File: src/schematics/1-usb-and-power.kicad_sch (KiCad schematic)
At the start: 0 parts

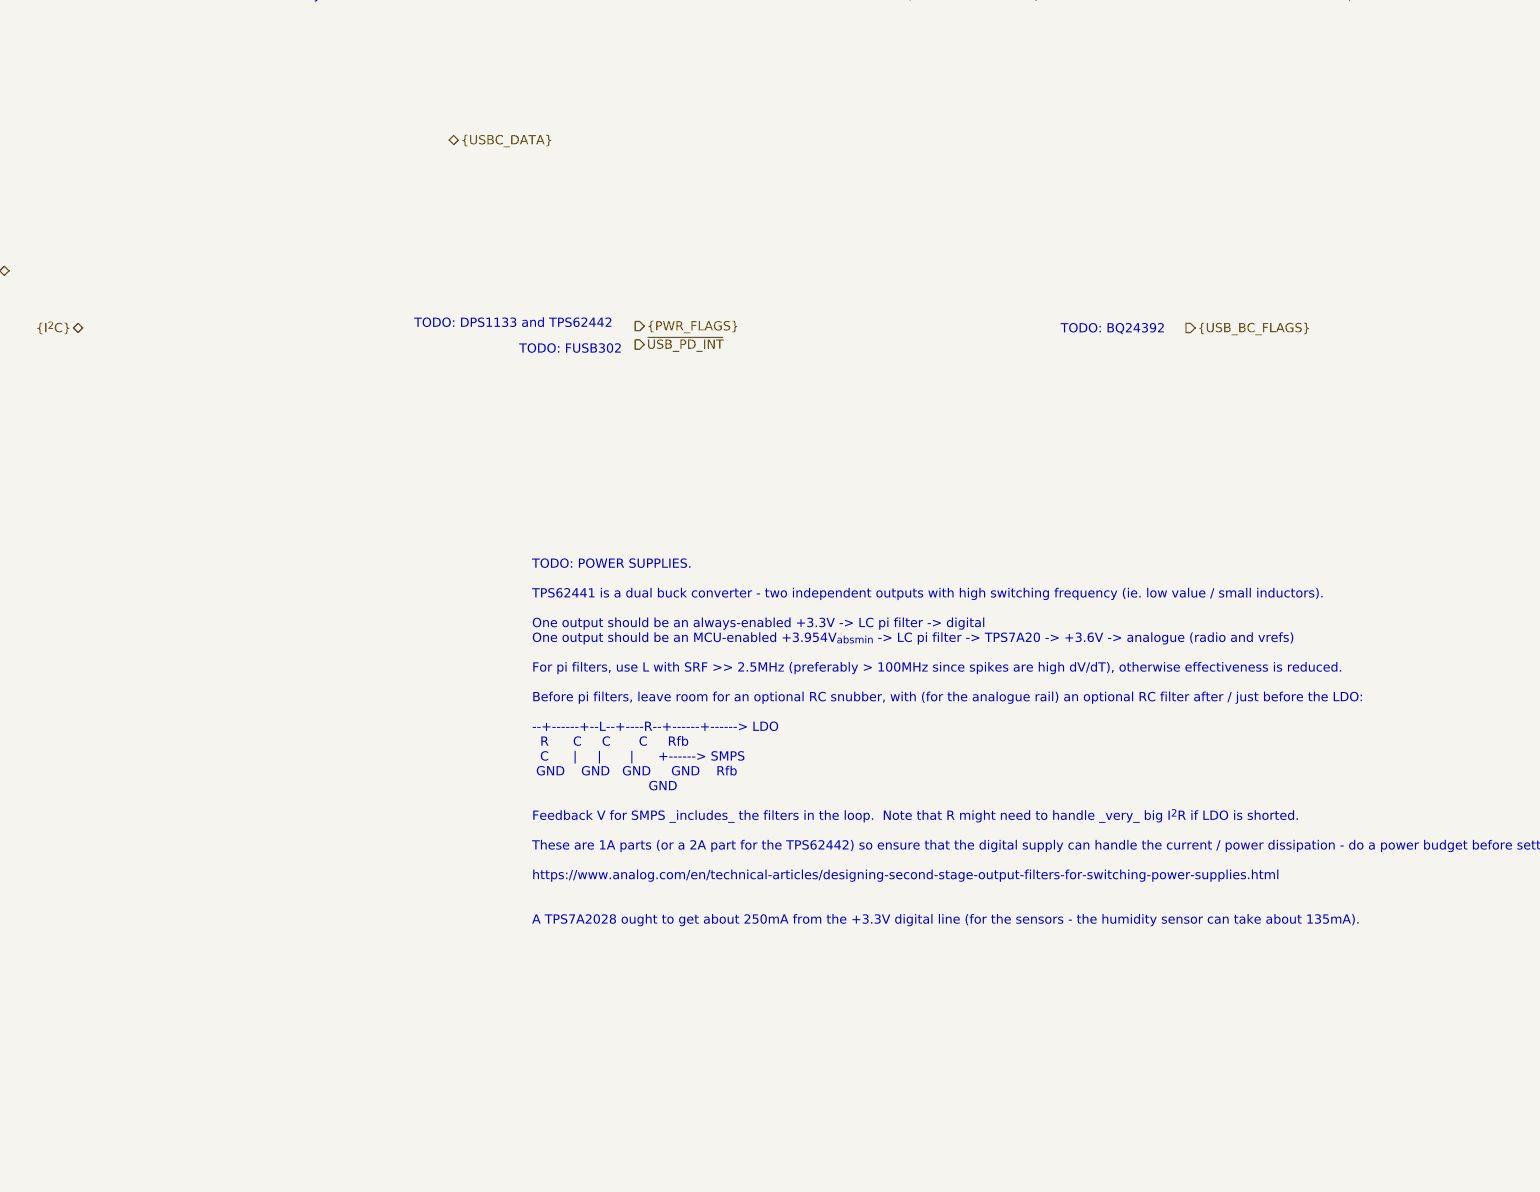
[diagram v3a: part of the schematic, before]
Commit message: Further elaboration of the design and schematics, mainly power supply calculations.
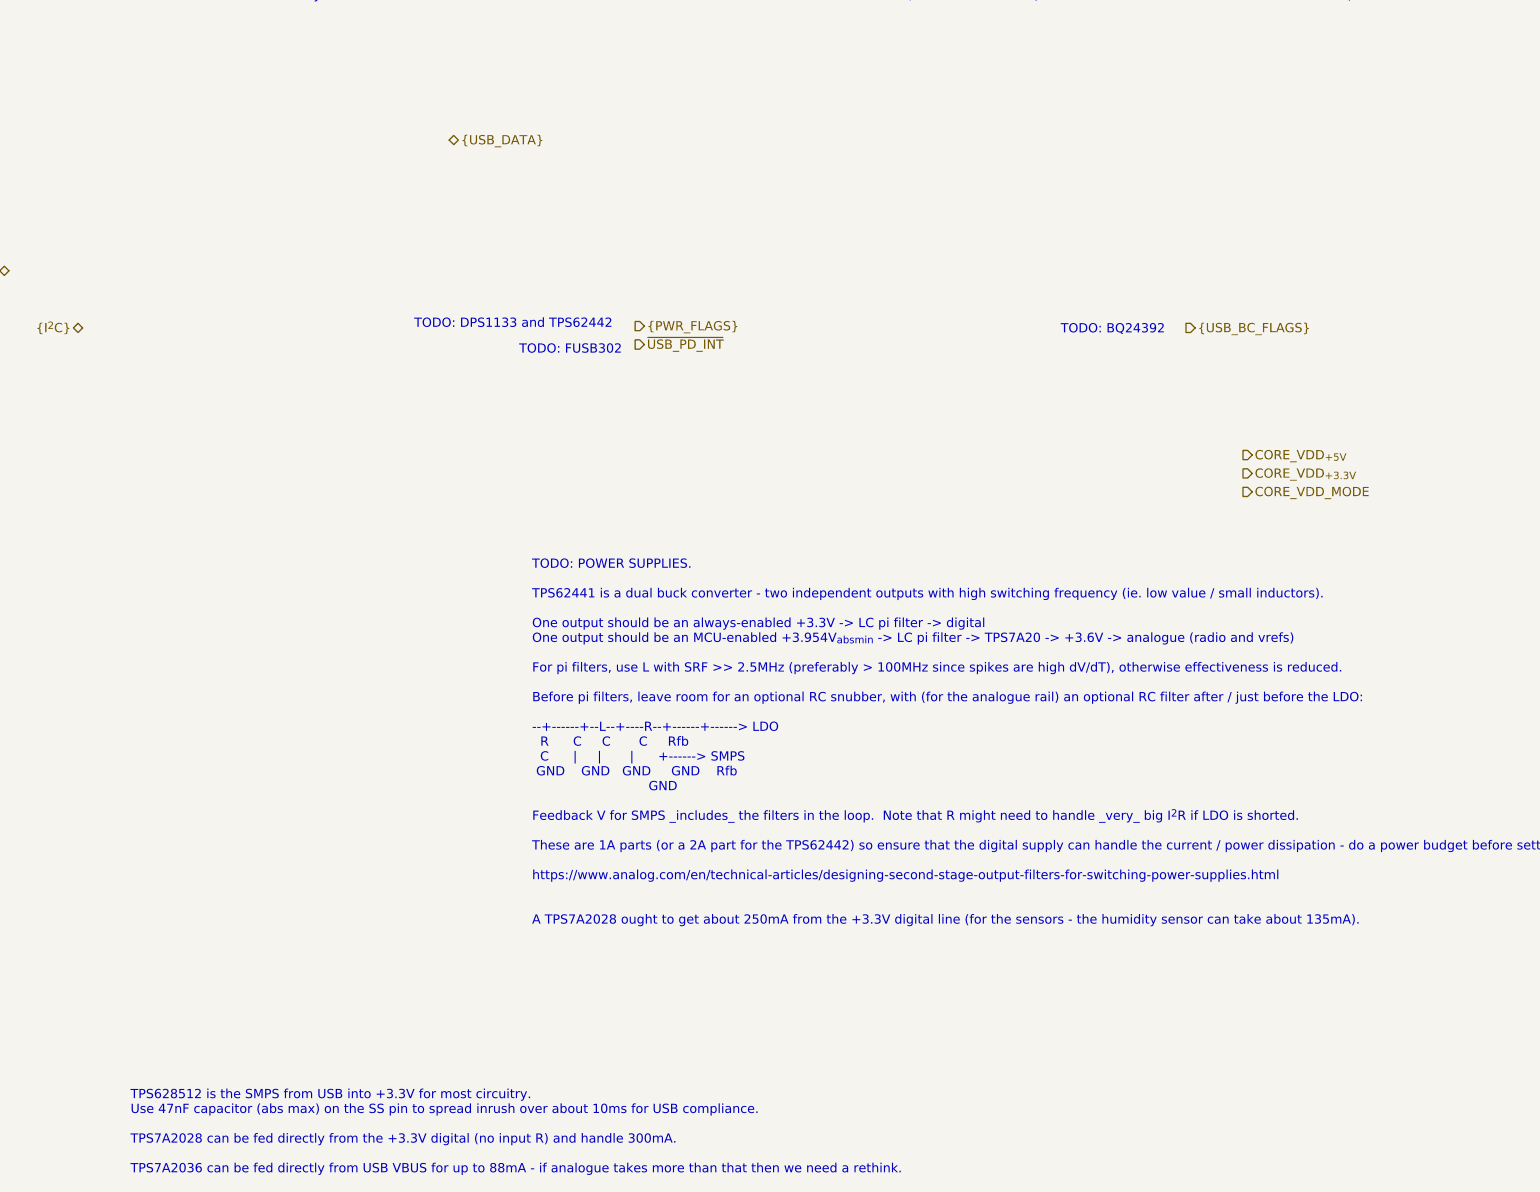
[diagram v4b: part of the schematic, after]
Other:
- note added: "TPS628512 is the SMPS from USB into +3.3V for most circuitry. Use 47nF capacitor (abs max) on the SS pin to spread inrush over about 10ms for USB compliance. TPS7A2028 can be fed directly from the +3.3V digital (no input R) and handle 300mA. TPS7A2036 can be fed directly from USB VBUS for up to 88mA - if analogue takes more than that then we need a rethink."
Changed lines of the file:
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@@
+    (effects (font (size 1.27 1.27)) (justify left bottom))
+  )
+  (text "TPS628512 is the SMPS from USB into +3.3V for most circuitry.\nUse 47nF capacitor (abs max) on the SS pin to spread inrush over about 10ms for USB compliance.\n\nTPS7A2028 can be fed directly from the +3.3V digital (no input R) and handle 300mA.\n\nTPS7A2036 can be fed directly from USB VBUS for up to 88mA - if analogue takes more than that then we need a rethink.\n"
+    (at 82.804 244.094 0)
     (effects (font (size 1.27 1.27)) (justify left bottom))
   )
@@
     (effects (font (size 1.27 1.27)) (justify right))
   )
-  (hierarchical_label "{USBC_DATA}" (shape bidirectional) (at 126.746 101.346 0) (fields_autoplaced)
+  (hierarchical_label "CORE_VDD_MODE" (shape output) (at 236.22 149.86 0) (fields_autoplaced)
     (effects (font (size 1.27 1.27)) (justify left))
   )
+  (hierarchical_label "CORE_VDD_{+3.3V}" (shape output) (at 236.22 147.32 0) (fields_autoplaced)
+    (effects (font (size 1.27 1.27)) (justify left))
+  )
+  (hierarchical_label "{USB_DATA}" (shape bidirectional) (at 126.746 101.346 0) (fields_autoplaced)
+    (effects (font (size 1.27 1.27)) (justify left))
+  )
+  (hierarchical_label "CORE_VDD_{+5V}" (shape output) (at 236.22 144.78 0) (fields_autoplaced)
+    (effects (font (size 1.27 1.27)) (justify left))
+  )

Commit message: Started to draw the USB / power input module.
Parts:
- added C23: 100nF, restall-generic-capacitors:unpolarised-nominal-0402-1005, symbol restall-generic-capacitors:capacitor-unpolarised
- added C24: DNP, restall-generic-capacitors:unpolarised-nominal-0402-1005, symbol restall-generic-capacitors:capacitor-unpolarised
- added C25: 360nF, restall-generic-capacitors:unpolarised-nominal-0402-1005, symbol restall-generic-capacitors:capacitor-unpolarised
- added C26: 100pF, restall-generic-capacitors:unpolarised-nominal-0402-1005, symbol restall-generic-capacitors:capacitor-unpolarised
- added C27, C28: 4.7μF, restall-generic-capacitors:unpolarised-nominal-0805-2012, symbol restall-generic-capacitors:capacitor-unpolarised
- added FB101: WLBD2012HCU121TH, restall-manufacturer-walsin:WLBD2012, symbol restall-manufacturer-walsin:WLBD2012HCU121TH
- added R21: 300kΩ, restall-generic-resistors:nominal-0402-1005, symbol restall-generic-resistors:resistor
- added R22: 0Ω, restall-generic-resistors:nominal-0402-1005, symbol restall-generic-resistors:resistor
- added R23: 1kΩ, restall-generic-resistors:nominal-0402-1005, symbol restall-generic-resistors:resistor
- added U2: MP5016HGQH, restall-manufacturer-mps:QFN10-1.5x2.0mm-0.5mm, symbol restall-manufacturer-mps:MP5016HGQH
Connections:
- net CORE_VDD_{+5V}: now also U2.6 (SOURCE)
- net USBC_VBUS: now also C27.1, FB101.1 (P1)
- new net: C26.1, U2.8 (GATE)
- new net: R23.1, U2.4 (ILIMIT)
- new net: C25.1, U2.10 (DV/DT)
- new net: C28.1, FB101.2 (P2), R21.1, U2.1 (V_{CC})
- new net: C23.1, R21.2, U2.9 (EN)
- new net: C24.1, R22.1, U2.5 (MODE)
- new net GND: C23.2, C24.2, C25.2, C26.2, C27.2, C28.2, R22.2, R23.2, U2.3 (GND)
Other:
- note added: "OVP_{typ}=5.75V [5.5V,6V] OCP_{typ}=2.1A"
- note added: "Ramp_{typ}=48ms; must be at least 20ms to keep USB inrush below 100mA"
- note added: "TODO: CHECK OCP LIMIT OF 2.1A IS SUFFICIENT FOR THE BUCK INDUCTOR CURRENT...WITH MARGIN !"
- note added: "TODO: OUTPUT CAPACITOR - TOTAL EFFECTIVE C ON THIS LINE MUST < 47uF"
- note removed: "TODO: Whilst the device will _support_ USB Suspend, it cannot actually achieve the 2.5mA limit - the DPS1133 voltage monitor / switch will draw a minimum of 1.5mA quiescent. What we can do - which seems to be compliant - is to issue a RESUME after 5ms of inactivity (3ms of inactivity triggers the SUSPEND). This is remote wake-up. It's not a particularly good thing to do since it requires hubs tha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"

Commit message: Further elaboration of the USB / Power schematic.
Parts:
- added C29, C32: 22μF, restall-generic-capacitors:unpolarised-nominal-0805-2012, symbol restall-generic-capacitors:capacitor-unpolarised
- added C30, C31: 4.7μF, restall-generic-capacitors:unpolarised-nominal-0402-1005, symbol restall-generic-capacitors:capacitor-unpolarised
- added C33, C34: ???pF, restall-generic-capacitors:unpolarised-nominal-0402-1005, symbol restall-generic-capacitors:capacitor-unpolarised
- added Q2: NX6008NBKW, restall-generic-sot:SOT-323, symbol restall-manufacturer-nexperia:NX6008NBKW
- added R24, R25: 2.2Ω, restall-generic-resistors:nominal-0402-1005, symbol restall-generic-resistors:resistor
- added R26, R27, R28: 33kΩ, restall-generic-resistors:nominal-0402-1005, symbol restall-generic-resistors:resistor
- added U3: BQ24392RSER, restall-manufacturer-ti:UQFN10-1.5x2.0mm-0.5mm, symbol restall-manufacturer-ti:BQ24392RSER
- added U4: FUSB302BMPX, restall-manufacturer-onsemi:WQFN14-2.5x2.5mm-0.5mm-expad-1.45x1.45mm-thermvias, symbol restall-manufacturer-onsemi:FUSB302BMPX
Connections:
- net CORE_VDD_{+5V}: now also C29.1, C30.1, C31.1, C32.1, U3.5 (GOOD_BAT), U3.9 (VBUS)
- net GND: now also C29.2, C30.2, C31.2, C32.2, C33.2, C34.2, Q2.2 (S), U3.6 (GND), U4.15 (GND), U4.8 (GND), U4.9 (GND)
- new net: U4.12 (VCONN), U4.13 (VCONN)
- new net: U4.3 (VDD), U4.4 (VDD)
- new net: R25.2, U3.8 (DM_CON)
- new net: Q2.1 (G), U3.10 (CHG_DET)
- new net: R24.2, U3.7 (DP_CON)
- new net CC1: C33.1, C34.1, U4.10 (CC1), U4.11 (CC1)
- new net CC2: U4.1 (CC2), U4.14 (CC2)
- new net D_{+}: R24.1, U3.3 (DP_HOST)
- new net D_{-}: R25.1, U3.2 (DM_HOST)
- new net ~{CHARGER_DETECTED}: Q2.3 (D), R28.2
- new net ~{CHARGING_ALLOWED}: R27.2, U3.4 (~{CHG_AL_N})
- new net ~{HAS_DATA}: R26.2, U3.1 (SW_OPEN)
- new net ~{USB_SUSPEND}: R26.1, R27.1, R28.1
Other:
- note added: "Between 4V-6V of DC bias, over temperature and at the extremes of tolerance, for C=22μF (CL21A226MPQNNN), 3.4μF<C_{eff}<12.2μF"
- note added: "Differential matched, Z_{diff}=90Ω"
- note added: "Keep C_{eff}≤47μF on CORE_VDD_{+5V} to meet USB inrush with 200μF behind the +3.3V buck regulator."
- note removed: "TODO: BQ24392"
- note removed: "TODO: OUTPUT CAPACITOR - TOTAL EFFECTIVE C ON THIS LINE MUST < 47uF"

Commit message: Further elaboration of the USB / Power schematic.
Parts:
- removed C32: 22μF, restall-generic-capacitors:unpolarised-nominal-0805-2012, symbol restall-generic-capacitors:capacitor-unpolarised
- added C35, C36: 100nF, restall-generic-capacitors:unpolarised-nominal-0402-1005, symbol restall-generic-capacitors:capacitor-unpolarised
- added C37, C38, C43, C44: 4.7μF, restall-generic-capacitors:unpolarised-nominal-0402-1005, symbol restall-generic-capacitors:capacitor-unpolarised
- added C40: 22μF, restall-generic-capacitors:unpolarised-nominal-0805-2012, symbol restall-generic-capacitors:capacitor-unpolarised
- added C41: 39pF, restall-generic-capacitors:unpolarised-nominal-0402-1005, symbol restall-generic-capacitors:capacitor-unpolarised
- added C42: 39nF, restall-generic-capacitors:unpolarised-nominal-0402-1005, symbol restall-generic-capacitors:capacitor-unpolarised
- added D8: diode, symbol restall-generic-diodes:diode
- added R30, R32: 33kΩ, restall-generic-resistors:nominal-0402-1005, symbol restall-generic-resistors:resistor
- added R31: 3.3kΩ, restall-generic-resistors:nominal-0402-1005, symbol restall-generic-resistors:resistor
- added R33: 1.8kΩ, restall-generic-resistors:nominal-0402-1005, symbol restall-generic-resistors:resistor
- added U6: TPS628512DRLR, restall-manufacturer-ti:SOT-583-8, symbol restall-manufacturer-ti:TPS62851?DRLR
- C25: value 360nF -> 100nF; Label 360nF±10% 10V X5R -> 100nF±20% 10V X5R; Tolerance ±10% -> ±20%
- C33, C34: value ???pF -> 470pF; Label ???pF±10% ??V C0G -> 470pF±10% 25V C0G; VoltageRating ??V -> 25V
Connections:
- net CC1: no longer C33.1
- net CC2: now also C33.1
- net CORE_VDD_MODE: now also R32.1, U6.3 (MODE)
- net CORE_VDD_{+3.3V}: now also U4.12 (VCONN), U4.13 (VCONN), U4.3 (VDD), U4.4 (VDD), C37.1, C38.1, R33.1
- net CORE_VDD_{+5V}: now also C40.1, C43.1, D8.1 (K), R30.1, U6.1 (V_{IN})
- net GND: now also C35.2, C36.2, C37.2, C38.2, C40.2, C41.2, C42.2, C43.2, C44.2, R32.2, U6.8 (GND)
- net ~{USB_PD_INT}: now also U4.5 (~{INT_N}), R33.2
- net at R23.1, U2.4 (ILIMIT): now also C41.1
- net USBC_VBUS_UNPROT: now reaches C28.1, FB101.2 (P2), R21.1, U2.1 (V_{CC})
- net USBC_VBUS_UNPROT: now also U4.2 (VBUS), C35.1, C36.1
- net SCL: now reaches U4.6 (SCL)
- net SDA: now reaches U4.7 (SDA)
- new net: C44.1, D8.2 (A), R30.2, U6.2 (EN)
- new net: C42.1, U6.4 (SS_TR)
- new net ~{CORE_VDD_FAULT}: R31.2, U6.6 (PG)
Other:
- note added: "Enable ~34ms, sufficient for USB inrush to settle from MP5016H ramp-up"
- note added: "Keep C_{eff}≤68μF on CORE_VDD_{+5V} to meet USB inrush with 200μF behind the +3.3V buck regulator."
- note added: "OCP_{typ}=2.1A"
- note added: "OVP_{typ}=5.75V [5.5V,6V]"
- note added: "Ramp_{typ}=13ms; must be at least 5ms to keep USB inrush steady below 100mA"
- note added: "Ramp_{typ}=9ms; must be at least 7ms to keep USB inrush steady below 100mA with C_{eff}≤200μF. Must be less than 16ms for MCU POR to operate correctly"
- note added: "TODO: CHECK OCP LIMIT OF 2.1A IS SUFFICIENT FOR THE BUCK INDUCTOR CURRENT (4A FOR 50ns)...WITH MARGIN !"
- note added: "TODO: SIMULATE CURRENT PULSES OF 4A FOR 50ns @ 2.25MHz ON THE INPUT BYPASS (FOR RIPPLE) AND ON THE STEADY-STATE CURRENT DRAWN FROM THE USB RAIL. IF THE CURRENT DRAWN FROM THE USB RAIL > THE MP5016H CURRENT LIMIT THEN IT WILL TRIP...NOT GOOD."
- note added: "TODO: TO BUCK OUTPUT..."
- note added: "TODO: VERIFY LABEL CORE_VDD_{+5V} AND HIERARCHY PIN OF SAME NAME ARE ACTUALLY THE SAME NET !"
- note removed: "Keep C_{eff}≤47μF on CORE_VDD_{+5V} to meet USB inrush with 200μF behind the +3.3V buck regulator."
- note removed: "OVP_{typ}=5.75V [5.5V,6V] OCP_{typ}=2.1A"
- note removed: "Ramp_{typ}=48ms; must be at least 20ms to keep USB inrush below 100mA"
- note removed: "TODO: CHECK OCP LIMIT OF 2.1A IS SUFFICIENT FOR THE BUCK INDUCTOR CURRENT...WITH MARGIN !"
- note removed: "TODO: DPS1133 and TPS62442"
- note removed: "TODO: FUSB302"
- note removed: "TODO: VCONN FOR FUSB302 - JUST TIE TO REGULATED 3.3V ALONG WITH VDD - NOT PARTICULARLY IMPORTANT FOR SINKS, THIS DOES WORK (HACKADAY ARTICLE ON USB PD DOES THE SAME)."
- note removed: "TPS628512 is the SMPS from USB into +3.3V for most circuitry. Use 47nF capacitor (abs max) on the SS pin to spread inrush over about 10ms for USB compliance. TPS7A2028 can be fed directly from the +3.3V digital (no input R) and handle 300mA. TPS7A2036 can be fed directly from USB VBUS for up to 88mA - if analogue takes more than that then we need a rethink."
- moved on the sheet: C23, C24, C27, C28, C31, FB101, Q2, R21, R22, R24, R25, R26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
